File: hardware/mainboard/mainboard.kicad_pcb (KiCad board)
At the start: 4 copper layers, 101.9 x 66.3 mm, 84 parts, among them J1 USB_C_Receptacle_USB2.0_16P, J2 Conn_01x03_Pin, J3 Barrel_Jack_MountingPin, J4 Conn_01x04_Socket, J5 Conn_01x04_Socket, J6 Screw_Terminal_01x02, J7 Conn_01x02_Socket, J8 Conn_01x02_Socket, J9 Conn_01x04_Socket, Q1 BTN8982TA, Q2 AO3400A, Q3 AO3400A, Q6 BTN8982TA, U1 ESP32-S3-WROOM-1, U2 USBLC6-2SC6, U3 AP2112K-3.3, U4 TPS2116DRL, U5 TPS62161DSG

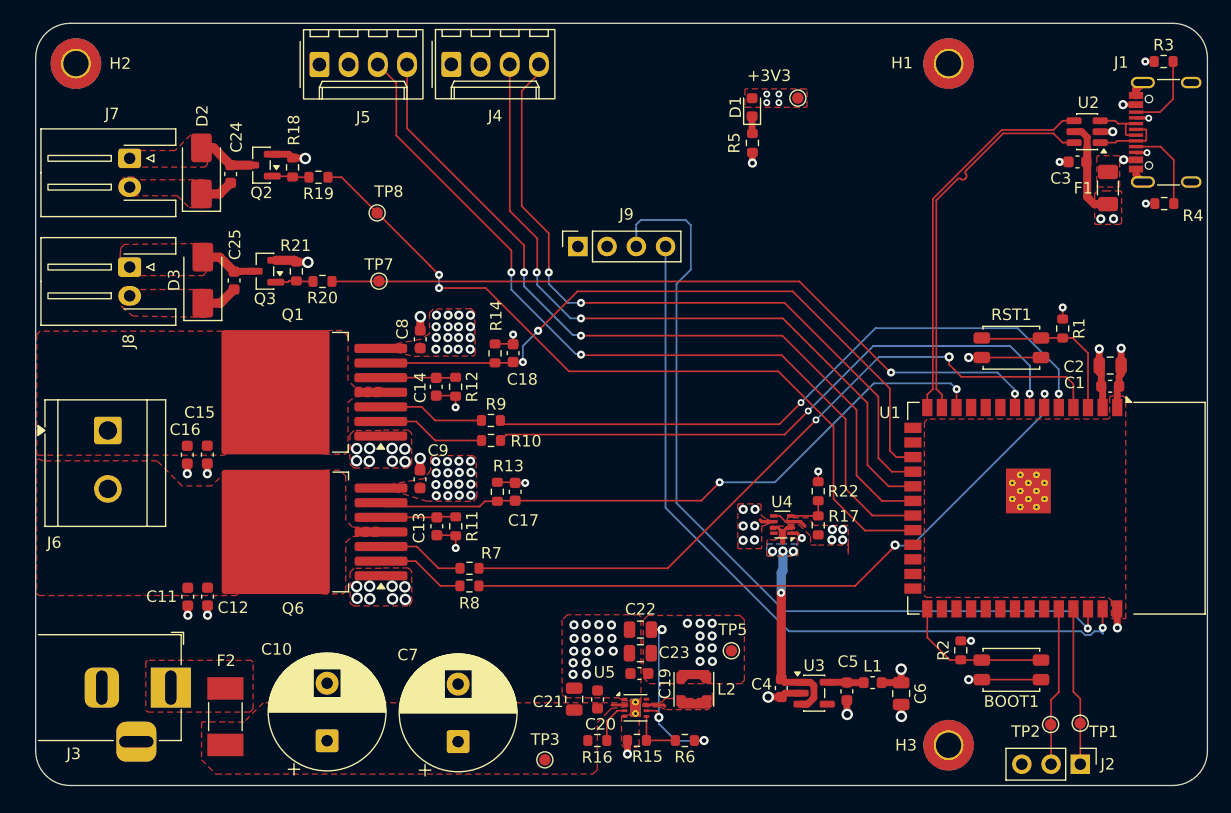
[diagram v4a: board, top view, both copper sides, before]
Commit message: added logo, routing fixes, added via stitching
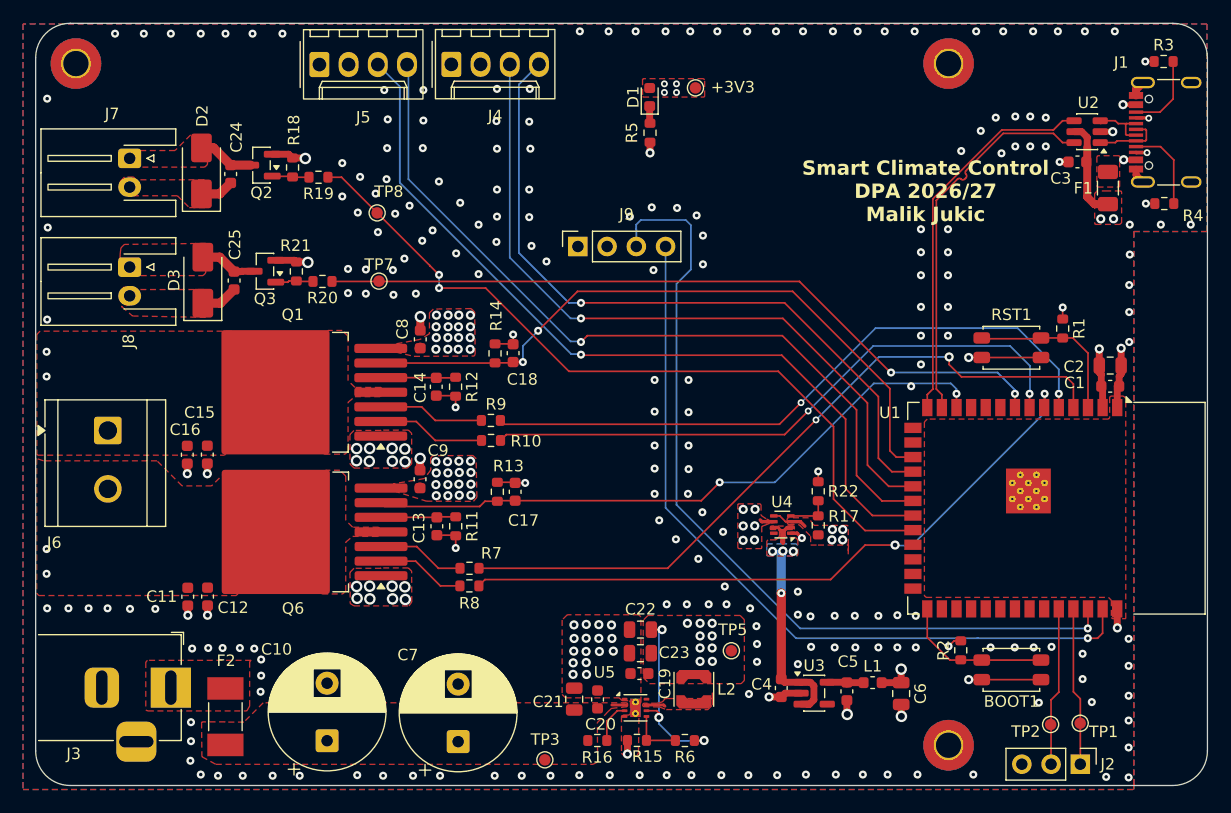
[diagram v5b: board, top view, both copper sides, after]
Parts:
- added G***: LOGO, Library:mmd_logo, B.Cu at (216.1, 65.5)
- moved D1 8.94 mm to (192.1, 56.2)
- moved R5 8.94 mm to (192.2, 59.3)
- moved TP6 8.94 mm to (196.1, 55.4)
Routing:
- net PWM2: track 68.3 -> 69.3 mm, vias 2 -> 1
- net TACH2: track 71.0 -> 71.2 mm, vias 2 -> 1
- net PWM1: track 62.2 -> 62.4 mm, vias 2 -> 1
- net TACH1: vias 2 -> 1
- net GND: vias 59 -> 269
- added copper zone on B.Cu, net GND
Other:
- board text added: "Smart Climate Control DPA 2026/27 Malik Jukic"

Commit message: routing reworks; adjusted display position, silkscreen adjustments
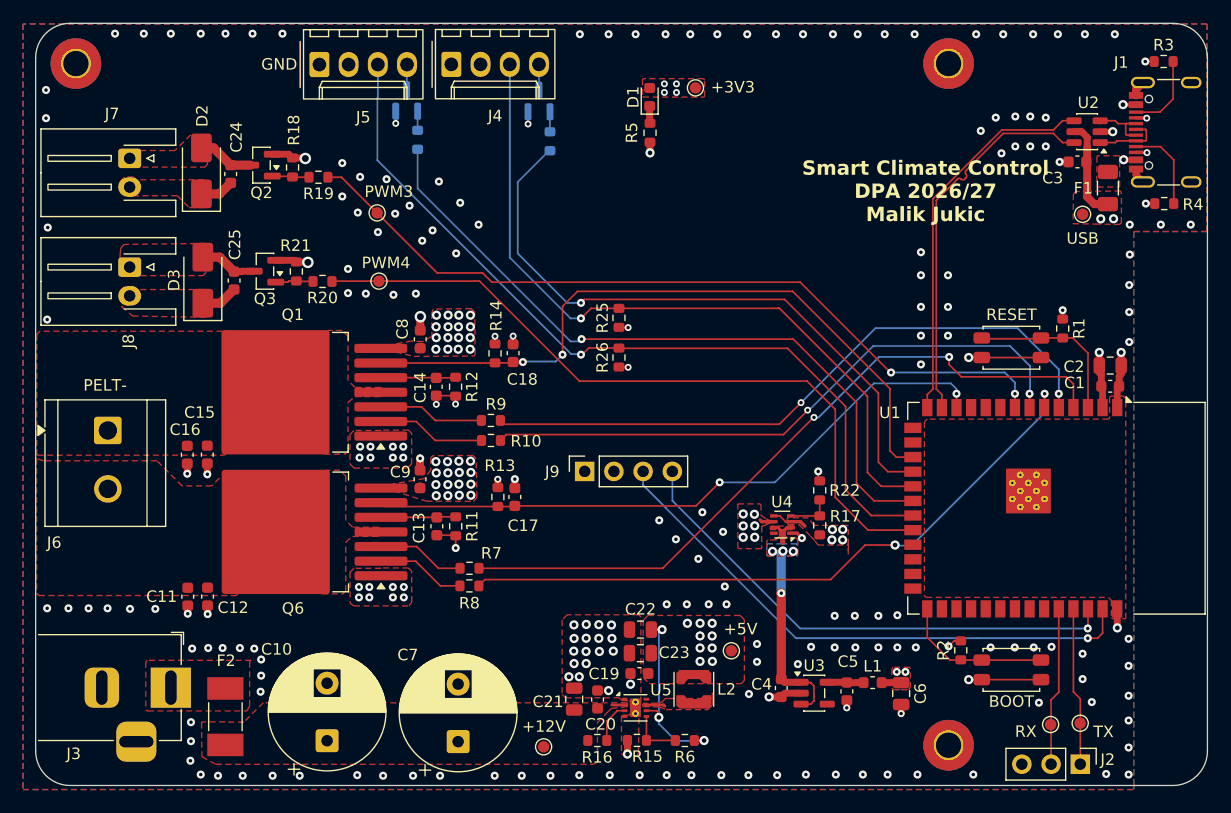
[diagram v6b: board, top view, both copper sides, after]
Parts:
- added Q4: AO3400A, Package_TO_SOT_SMD:SOT-23, B.Cu at (171.0, 56.5)
- added Q5: AO3400A, Package_TO_SOT_SMD:SOT-23, B.Cu at (182.5, 56.5)
- added R23: 220, Resistor_SMD:R_0603_1608Metric, B.Cu at (171.9, 59.9)
- added R24: 220, Resistor_SMD:R_0603_1608Metric, B.Cu at (183.4, 60.0)
- added R25: 10k, Resistor_SMD:R_0603_1608Metric, F.Cu at (189.4, 75.4)
- added R26: 10k, Resistor_SMD:R_0603_1608Metric, F.Cu at (189.4, 78.8)
- added USB: TestPoint_VBUS, TestPoint:TestPoint_Pad_D1.0mm, F.Cu at (229.8, 66.4)
- moved J9 19.6 mm to (186.5, 88.8)
- moved +12V 1.14 mm to (182.9, 112.7)
- moved R13 0.46 mm to (178.9, 91.0)
- moved C17 0.46 mm to (180.4, 91.0)
- moved R22 0.15 mm to (206.9, 90.4)
- moved R17 0.13 mm to (206.9, 93.4)
- renumbered TP3 to +12V, TP5 to +5V, BOOT1 to BOOT, TP8 to PWM3, TP7 to PWM4, RST1 to RESET, TP2 to RX, TP1 to TX
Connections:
- net /GATE renamed /FAN_GATE
- net /GATE2 renamed /FAN_GATE2
- J4 pad 4: PWM1 -> /PWM1_OUT
- J5 pad 4: PWM2 -> /PWM2_OUT
- U1 pad 22: PWM3 -> PWM4
- U1 pad 38: SCL -> SDA
- U1 pad 39: SDA -> SCL
- U1 pad 8: PWM4 -> PWM3
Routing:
- net SCL: track 73.7 -> 49.4 mm
- net SDA: track 67.7 -> 45.3 mm
- net PWM2: track 69.3 -> 62.0 mm
- net PWM1: track 62.4 -> 56.1 mm
- net /PWM1_OUT: track 0.00 -> 2.74 mm
- net /PWM2_OUT: track 0.00 -> 2.62 mm
- net /GATE1: track 0.00 -> 1.74 mm
- net /GATE2: track 0.00 -> 1.66 mm
- net IS_2: track 58.8 -> 60.4 mm
- net TACH1: track 63.6 -> 65.0 mm
- net PWM3: track 68.0 -> 69.3 mm
- net TACH2: track 71.2 -> 72.4 mm
- net GND: track 57.0 -> 55.8 mm, vias 269 -> 221
- net PWM4: track 64.8 -> 64.0 mm, vias 2 -> 0
- net +3V3: track 10.3 -> 10.2 mm, vias 8 -> 11
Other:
- board text added: "GND"
- board text added: "PELT-"

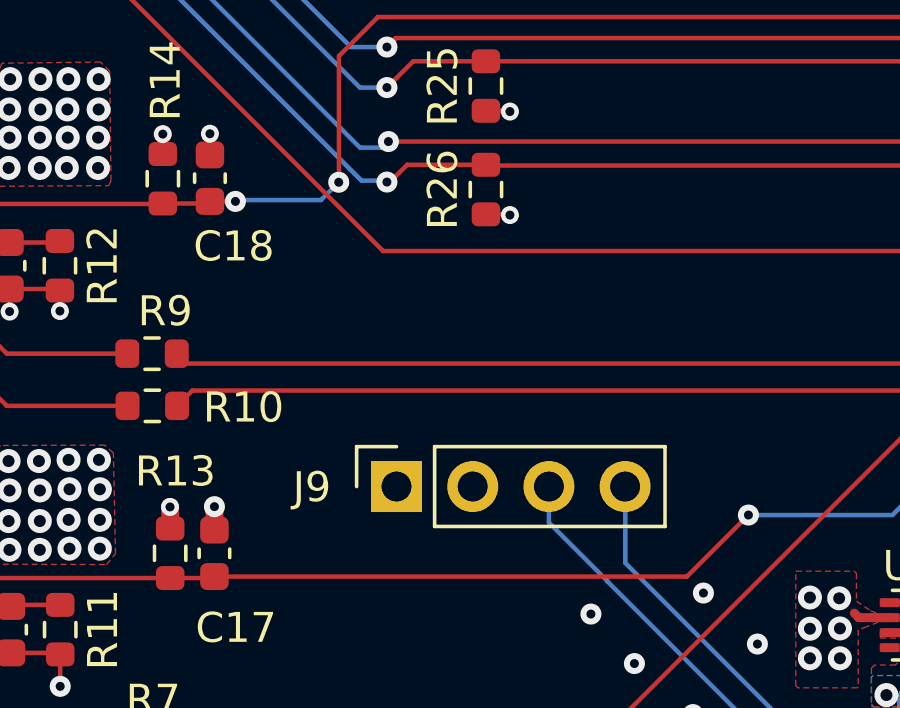
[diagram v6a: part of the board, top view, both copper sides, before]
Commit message: added doc to docs, adjustemnt to display positioning
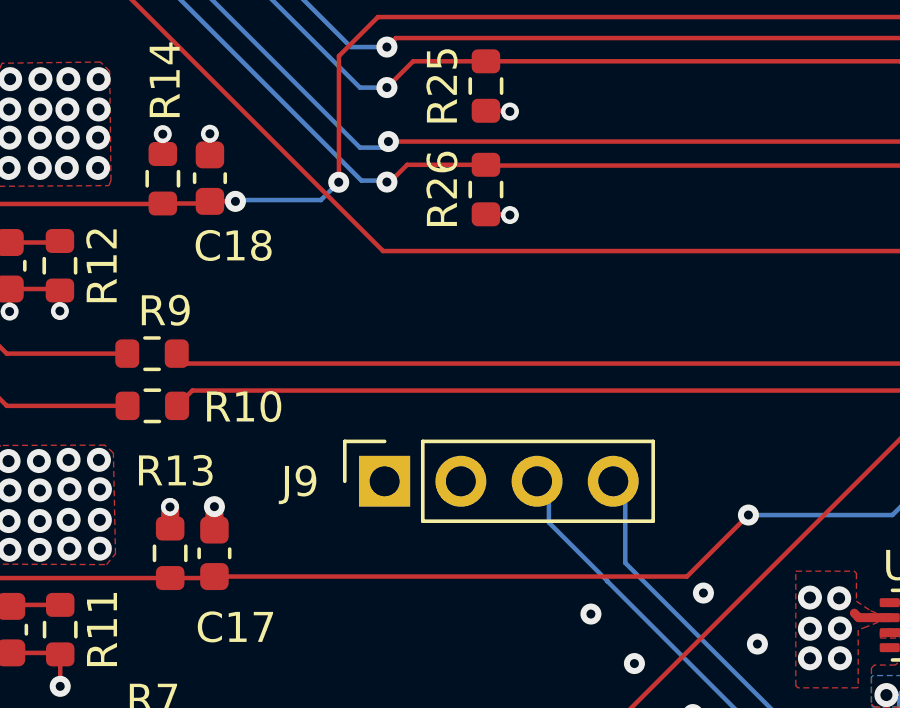
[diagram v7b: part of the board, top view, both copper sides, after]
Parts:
- moved J9 0.43 mm to (186.1, 88.6)
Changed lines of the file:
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@@
 	(footprint "Connector_PinSocket_2.54mm:PinSocket_1x04_P2.54mm_Vertical"
 		(layer "F.Cu")
-		(at 186.47 88.75 90)
+		(at 186.075 88.575 90)
 		(descr "Through hole straight socket strip, 1x04, 2.54mm pitch, single row (from Kicad 4.0.7), script generated")
 		(tags "Through hole socket strip THT 1x04 2.54mm single row")
@@
 	)
 	(gr_rect
-		(start 177.24 64.97)
-		(end 203.3 90.97)
+		(start 176.875 64.775)
+		(end 202.935 90.775)
 		(stroke
 			(width 0.1)
@@
 		(layer "F.Fab")
 		(pts
+			(xy 176.875 90.775) (xy 189.875 88.6)
+		)
+		(height 5.135)
+		(orientation 0)
+		(format
+			(prefix "")
+			(suffix "")
+			(units 3)
+			(units_format 0)
+			(precision 4)
+			(suppress_zeroes yes)
+		)
+		(style
+			(thickness 0.1)
+			(arrow_length 1.27)
+			(text_position_mode 0)
+			(arrow_direction outward)
+			(extension_height 0.58642)
+			(extension_offset 0.5)
+			(keep_text_aligned yes)
+		)
+		(gr_text "13"
+			(at 183.375 94.76 0)
+			(layer "F.Fab")
+			(effects
+				(font
+					(size 1 1)
+					(thickness 0.15)
+				)
+			)
+		)
+	)
+	(dimension
+		(type orthogonal)
+		(layer "F.Fab")
+		(pts
 			(xy 240.6 52.8) (xy 218.1 52.8)
 		)
@@
 		(layer "F.Fab")
 		(pts
-			(xy 177.24 64.97) (xy 177.24 49.79)
+			(xy 184.13 90.8) (xy 184.07 88.6)
 		)
-		(height -42.12)
+		(height -1.98)
 		(orientation 1)
 		(format
@@
 			(keep_text_aligned yes)
 		)
-		(gr_text "15,18"
-			(at 133.97 57.38 90)
+		(gr_text "2,2"
+			(at 181 89.7 90)
 			(layer "F.Fab")
 			(effects
@@
 		(layer "F.Fab")
 		(pts
-			(xy 177.24 64.97) (xy 138.82 65.01)
+			(xy 176.875 64.775) (xy 138.82 65.01)
 		)
-		(height -18.41)
+		(height -18.44)
 		(orientation 0)
 		(format
@@
 			(keep_text_aligned yes)
 		)
-		(gr_text "38,42"
-			(at 158.03 45.41 0)
+		(gr_text "38,055"
+			(at 157.8475 45.185 0)
 			(layer "F.Fab")
 			(effects
@@
 	)
 	(segment
-		(start 181.1 79.245)
-		(end 180.25 79.245)
+		(start 178.68 79.315)
+		(end 180.18 79.315)
 		(width 0.15)
 		(layer "F.Cu")
@@
 	)
 	(segment
-		(start 178.68 79.315)
-		(end 180.18 79.315)
+		(start 181.1 79.245)
+		(end 180.25 79.245)
 		(width 0.15)
 		(layer "F.Cu")
@@
 	(segment
 		(start 183.95 79.2)
-		(end 181.145 79.2)
+		(end 184.543413 78.606587)
 		(width 0.15)
 		(layer "B.Cu")
@@
 	)
 	(segment
-		(start 184.543413 78.606587)
+		(start 181.145 79.2)
 		(end 183.95 79.2)
 		(width 0.15)
@@
 	)
 	(segment
-		(start 181.145 79.2)
-		(end 181.1 79.245)
+		(start 181.1 79.245)
+		(end 181.145 79.2)
 		(width 0.15)
 		(layer "B.Cu")

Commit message: continued documentation
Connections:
- J3 pad 3: (no net) -> GND
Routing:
- net GND: vias 221 -> 215
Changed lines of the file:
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@@
 			(remove_unused_layers no)
 			(roundrect_rratio 0.25)
+			(net 2 "GND")
 		)
 		(embedded_fonts no)
@@
 		(layer "F.Fab")
 		(pts
-			(xy 176.875 90.775) (xy 189.875 88.6)
+			(xy 176.875 90.775) (xy 202.94 87.85)
 		)
-		(height 5.135)
+		(height 2.475)
 		(orientation 0)
 		(format
@@
 			(keep_text_aligned yes)
 		)
-		(gr_text "13"
-			(at 183.375 94.76 0)
+		(gr_text "26,065"
+			(at 189.9075 92.1 0)
 			(layer "F.Fab")
 			(effects
@@
 	)
 	(via
-		(at 175.65 65.4)
-		(size 0.7)
-		(drill 0.3)
-		(layers "F.Cu" "B.Cu")
-		(free yes)
-		(net 2)
-	)
-	(via
 		(at 148.15 50.7)
 		(size 0.7)
@@
 	)
 	(via
-		(at 169.25 63.35)
-		(size 0.7)
-		(drill 0.3)
-		(layers "F.Cu" "B.Cu")
-		(free yes)
-		(net 2)
-	)
-	(via
 		(at 152.35 104.15)
 		(size 0.7)
@@
 	)
 	(via
-		(at 177.25 67.3)
-		(size 0.7)
-		(drill 0.3)
-		(layers "F.Cu" "B.Cu")
-		(free yes)
-		(net 2)
-	)
-	(via
 		(at 194.4 94.65)
 		(size 0.7)
@@
 	)
 	(via
-		(at 173.25 67.8)
-		(size 0.7)
-		(drill 0.3)
-		(layers "F.Cu" "B.Cu")
-		(free yes)
-		(net 2)
-	)
-	(via
 		(at 168.95 115.2)
 		(size 0.7)
@@
 	)
 	(via
-		(at 173.8 63.55)
-		(size 0.7)
-		(drill 0.3)
-		(layers "F.Cu" "B.Cu")
-		(free yes)
-		(net 2)
-	)
-	(via
 		(at 210 104.05)
 		(size 0.7)
@@
 	)
 	(via
-		(at 171.25 65.65)
-		(size 0.7)
-		(drill 0.3)
-		(layers "F.Cu" "B.Cu")
-		(free yes)
-		(net 2)
-	)
-	(via
 		(at 165.9 71.15)
 		(size 0.7)
@@
 	)
 	(segment
-		(start 205.2 102.4)
-		(end 194.095 91.295)
+		(start 193.695 90.895)
+		(end 193.695 88.775)
 		(width 0.15)
 		(layer "B.Cu")
@@
 	)
 	(segment
-		(start 194.095 91.295)
-		(end 194.095 88.375)
+		(start 205.2 102.4)
+		(end 193.695 90.895)
 		(width 0.15)
 		(layer "B.Cu")
@@
 	)
 	(segment
-		(start 193.5 91.9)
-		(end 191.55 89.95)
+		(start 219.474 103.25)
+		(end 204.840412 103.25)
 		(width 0.15)
 		(layer "B.Cu")
@@
 	)
 	(segment
-		(start 220.626 103.236412)
-		(end 220.612412 103.25)
+		(start 230.2 103.25)
+		(end 220.626 103.25)
 		(width 0.15)
 		(layer "B.Cu")
@@
 	)
 	(segment
-		(start 220.626 103.25)
-		(end 220.626 103.236412)
+		(start 192.69 90.06)
+		(end 191.18 88.55)
 		(width 0.15)
 		(layer "B.Cu")
@@
 	)
 	(segment
-		(start 230.2 103.25)
-		(end 220.626 103.25)
+		(start 220.626 103.25)
+		(end 220.626 103.236412)
 		(width 0.15)
 		(layer "B.Cu")
@@
 	)
 	(segment
-		(start 193.5 91.909588)
-		(end 193.5 91.9)
+		(start 204.840412 103.25)
+		(end 192.69 91.099588)
 		(width 0.15)
 		(layer "B.Cu")
@@
 	)
 	(segment
-		(start 204.840412 103.25)
-		(end 193.5 91.909588)
+		(start 220.626 103.236412)
+		(end 220.612412 103.25)
 		(width 0.15)
 		(layer "B.Cu")
@@
 	)
 	(segment
-		(start 191.55 88.38)
-		(end 191.555 88.375)
+		(start 219.487588 103.25)
+		(end 219.474 103.236412)
 		(width 0.15)
 		(layer "B.Cu")
@@
 	)
 	(segment
-		(start 191.55 89.95)
-		(end 191.55 88.38)
-		(width 0.15)
-		(layer "B.Cu")
-		(net 29)
-	)
-	(segment
-		(start 219.487588 103.25)
-		(end 219.474 103.236412)
-		(width 0.15)
-		(layer "B.Cu")
-		(net 29)
-	)
-	(segment
-		(start 219.474 103.25)
-		(end 204.840412 103.25)
+		(start 192.69 91.099588)
+		(end 192.69 90.06)
 		(width 0.15)
 		(layer "B.Cu")
